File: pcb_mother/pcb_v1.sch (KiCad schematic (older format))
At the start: 32 parts, among them J1 Conn_01x02, J10 Conn_01x02, J11 Conn_01x06, J12 Conn_01x02, J13 Conn_01x02, J14 Conn_01x06, J3 Conn_01x02, J4 Conn_01x02_Male, J5 Conn_01x02_Male, J6 Conn_01x02, J7 Conn_01x01, J8 Conn_01x01, J9 Conn_01x02, Q10 2N2219, Q11 2N2219, Q12 2N2219, Q13 2N2219, Q14 2N2219, U1 TB6612F, U2 Rws433mhz, U3 tws

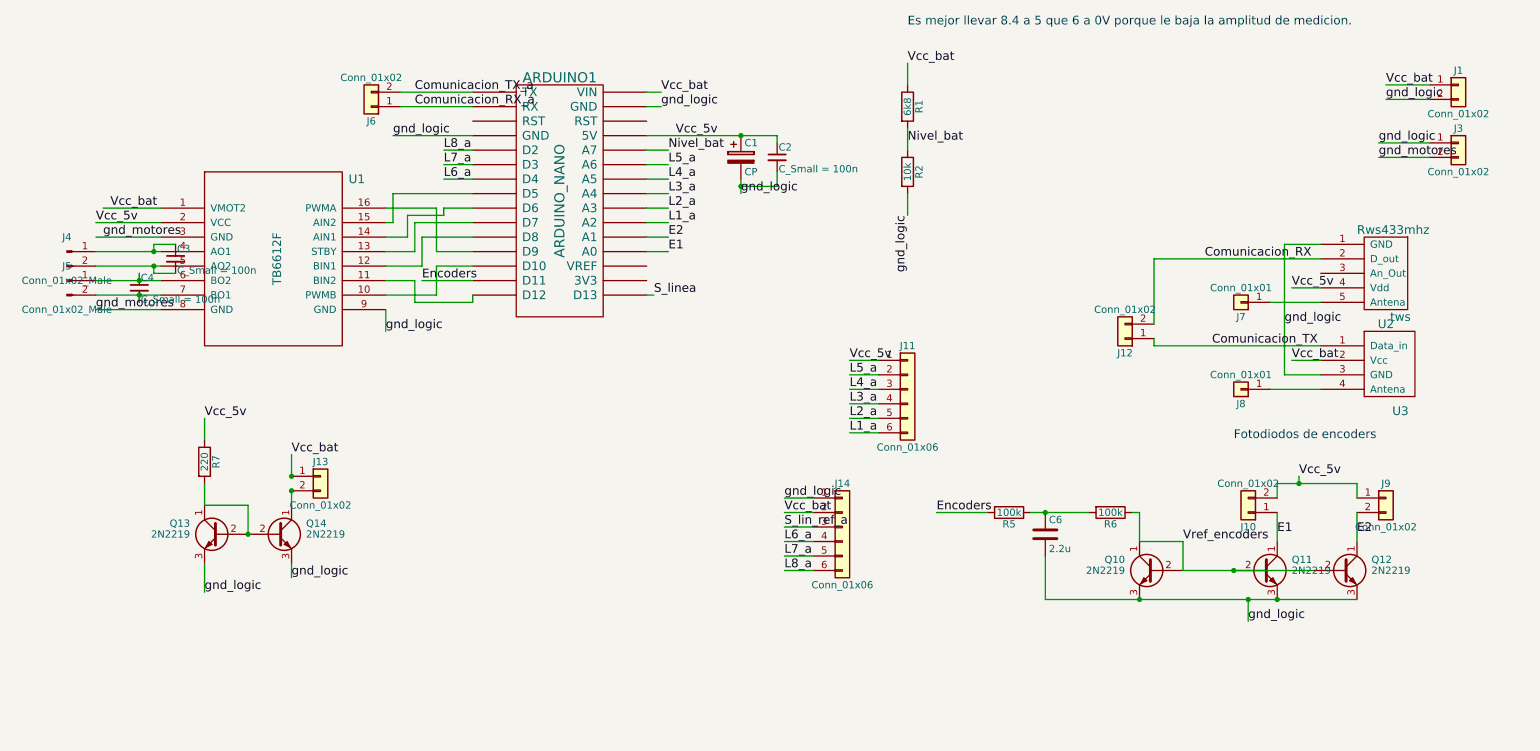
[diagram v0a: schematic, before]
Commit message: Se moifico el esquematico y se esta acomodando para poder armar el pcb, la linea que se va a seguir es priorizar el funcionamiento antes que la estetica y el espacio.
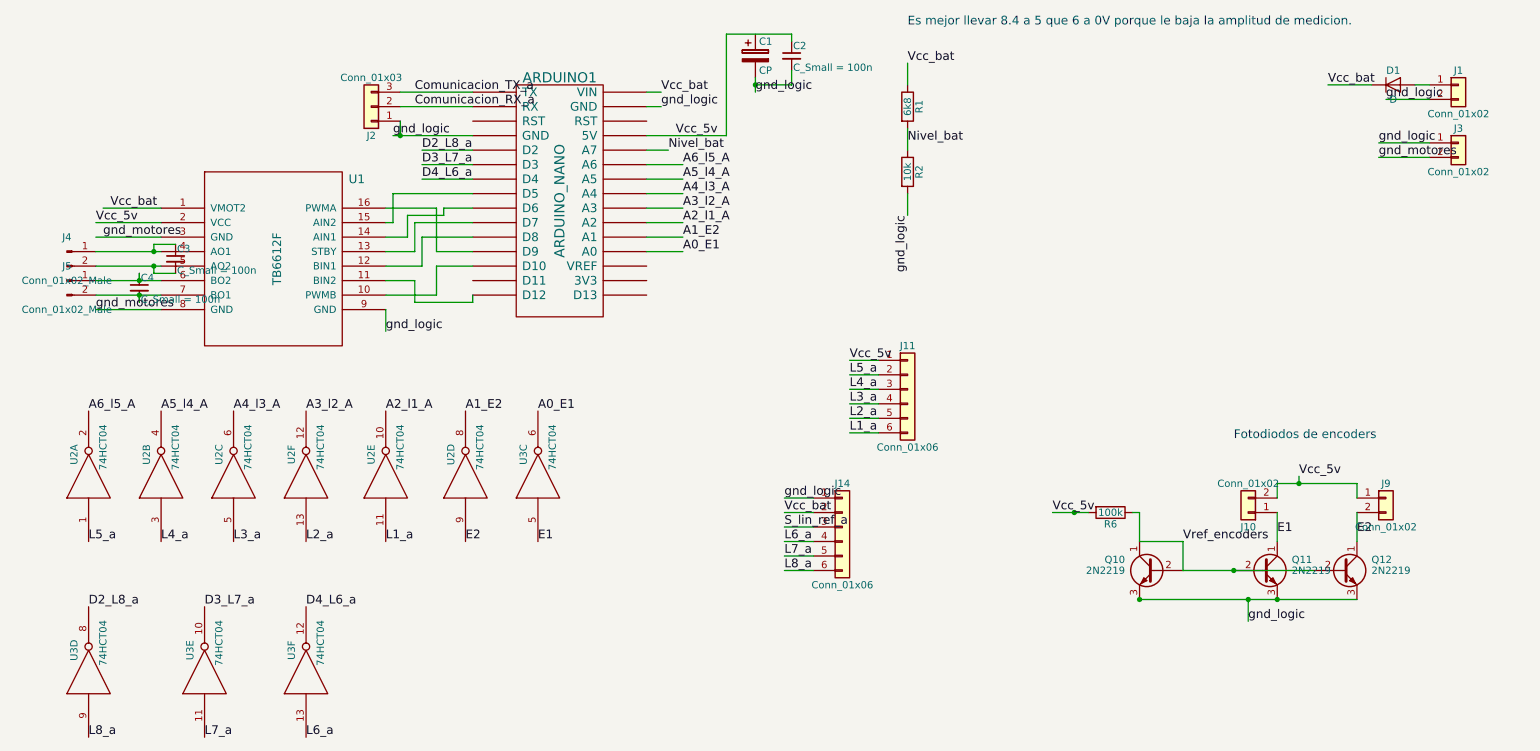
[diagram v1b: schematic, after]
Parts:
- removed C6: 2.2u, Capacitors_THT:CP_Radial_D5.0mm_P2.50mm, symbol C
- removed J12, J13, J6: Conn_01x02, Pin_Headers:Pin_Header_Straight_1x02_Pitch2.54mm, symbol Conn_01x02
- removed J7, J8: Conn_01x01, Pin_Headers:Pin_Header_Straight_1x01_Pitch2.54mm, symbol Conn_01x01
- removed Q13, Q14: 2N2219, TO_SOT_Packages_THT:TO-92_Inline_Wide, symbol BC548
- removed R5: 100k, Resistors_THT:R_Axial_DIN0207_L6.3mm_D2.5mm_P10.16mm_Horizontal, symbol R
- removed R7: 220, Resistors_THT:R_Axial_DIN0207_L6.3mm_D2.5mm_P10.16mm_Horizontal, symbol R
- removed U2: Rws433mhz, Propias:rws433, symbol Rws433mhz
- removed U3: tws, Propias:tws433, symbol tws
- added D1: D, Diodes_SMD:D_1206, symbol D
- added J2: Conn_01x03, Pin_Headers:Pin_Header_Straight_1x03_Pitch2.54mm, symbol Conn_01x03
- added U2, U3: 74HCT04, Housings_DIP:DIP-14_W7.62mm_Socket_LongPads, symbol 74HCT04
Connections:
- net Comunicacion_RX_a: now also J2.2 (Pin_2)
- net Comunicacion_TX_a: now also J2.3 (Pin_3)
- net E1: now also U3.5; no longer ARDUINO1.19 (A0)
- net E2: now also U2.9; no longer ARDUINO1.20 (A1)
- net L1_a: now also U2.11; no longer ARDUINO1.21 (A2)
- net L2_a: now also U2.13; no longer ARDUINO1.22 (A3)
- net L3_a: now also U2.5; no longer ARDUINO1.23 (A4)
- net L4_a: now also U2.3; no longer ARDUINO1.24 (A5)
- net L5_a: now also U2.1; no longer ARDUINO1.25 (A6)
- net L6_a: now also U3.13; no longer ARDUINO1.7 (D4)
- net L7_a: now also U3.11; no longer ARDUINO1.6 (D3)
- net L8_a: now also U3.9; no longer ARDUINO1.5 (D2)
- net Vcc_5v: now also R6.2; no longer C1.1
- net Vcc_bat: now also D1.1 (K); no longer J1.1 (Pin_1)
- net gnd_logic: now also J2.1 (Pin_1)
- net Encoders: no longer names the net of ARDUINO1.14 (D11)
- net S_linea: no longer names the net of ARDUINO1.16 (D13)
- new net: D1.2 (A), J1.1 (Pin_1)
- new net A0_E1: ARDUINO1.19 (A0), U3.6
- new net A1_E2: ARDUINO1.20 (A1), U2.8
- new net A2_l1_A: ARDUINO1.21 (A2), U2.10
- new net A3_l2_A: ARDUINO1.22 (A3), U2.12
- new net A4_l3_A: ARDUINO1.23 (A4), U2.6
- new net A5_l4_A: ARDUINO1.24 (A5), U2.4
- new net A6_l5_A: ARDUINO1.25 (A6), U2.2
- new net D2_L8_a: ARDUINO1.5 (D2), U3.8
- new net D3_L7_a: ARDUINO1.6 (D3), U3.10
- new net D4_L6_a: ARDUINO1.7 (D4), U3.12
- new net GND: U2.7 (GND), U2.7 (GND), U2.7 (GND), U2.7 (GND), U2.7 (GND), U2.7 (GND), U3.7 (GND), U3.7 (GND), U3.7 (GND), U3.7 (GND)
- new net VCC: U2.14 (VCC), U2.14 (VCC), U2.14 (VCC), U2.14 (VCC), U2.14 (VCC), U2.14 (VCC), U3.14 (VCC), U3.14 (VCC), U3.14 (VCC), U3.14 (VCC)
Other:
- moved on the sheet: C1, C2

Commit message: Se pudiron acomodar los inversores, ahora falta poner el divisor resistivo, los planos de tierra, los puentes y los aujeros...
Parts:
- renumbered U2 to U3
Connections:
- net Vcc_5v is gone; now on net VCC: ARDUINO1.27 (5V), C2.1, J10.2 (Pin_2), J11.1 (Pin_1), J9.1 (Pin_1), R6.2, U1.2 (VCC)
- net A0_E1: now also U3.4; no longer U3.6
- net A1_E2: now also U3.6; no longer U3.8
- net E1: now also J9.2 (Pin_2), Q12.1 (C); no longer J10.1 (Pin_1), Q11.1 (C)
- net E2: now also J10.1 (Pin_1), Q11.1 (C), U3.3; no longer J9.2 (Pin_2), Q12.1 (C), U3.9
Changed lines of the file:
@@
 	9600 4050 9600 4250
 Connection ~ 9050 4650
-Text Label 9600 4200 0    60   ~ 0
+Text Label 9050 4150 0    60   ~ 0
 E2
-Text Label 9050 4200 0    60   ~ 0
+Text Label 9600 4150 0    60   ~ 0
 E1
 $Comp
@@
 Text Label 2900 3350 0    60   ~ 0
 A2_l1_A
+Text Label 3950 3350 0    60   ~ 0
+A1_E2
 Text Label 3450 3350 0    60   ~ 0
-A1_E2
-Text Label 3950 3350 0    60   ~ 0
 A0_E1
 Text Label 850  4700 0    60   ~ 0
@@
 $EndComp
 $Comp
-L 74HCT04 U2
-U 4 1 5AF29DC5
+L 74HCT04 U3
+U 2 1 5AF29DC5
 P 3450 3800
-F 0 "U2" H 3600 3900 50  0000 C CNN
+F 0 "U3" H 3600 3900 50  0000 C CNN
 F 1 "74HCT04" H 3650 3700 50  0000 C CNN
 F 2 "Housings_DIP:DIP-14_W7.62mm_Socket_LongPads" H 3450 3800 50  0001 C CNN
 F 3 "" H 3450 3800 50  0001 C CNN
-	4    3450 3800
+	2    3450 3800
 	0    -1   -1   0
 $EndComp
@@
 Text Label 4950 1650 0    60   ~ 0
 A6_l5_A
+Text Label 5250 1450 0    60   ~ 0
+VCC
 $EndSCHEMATC

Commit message: Casi termino la placa, falta el plano de tierra, algunos puentes y los aujeros de montaje.
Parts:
- C1: value CP -> 10u
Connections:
- net gnd_logic is gone; now on net GND: ARDUINO1.29 (GND), ARDUINO1.4 (GND), C1.2, C2.2, J1.2 (Pin_2), J14.1 (Pin_1), J2.1 (Pin_1), J3.1 (Pin_1), Q10.3 (E), Q11.3 (E), Q12.3 (E), R2.2, U1.9 (GND)
- net VCC: now also C1.1
- net S_lin_ref_a: no longer names the net of J14.3 (Pin_3)
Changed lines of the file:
@@
 P 5450 900
 F 0 "C1" H 5475 1000 50  0000 L CNN
-F 1 "CP" H 5475 800 50  0000 L CNN
+F 1 "10u" H 5475 800 50  0000 L CNN
 F 2 "Capacitors_THT:CP_Radial_D5.0mm_P2.50mm" H 5488 750 50  0001 C CNN
 F 3 "" H 5450 900 50  0001 C CNN
@@
 Wire Wire Line
 	6100 3200 6300 3200
-Text Label 5650 4150 0    60   ~ 0
-S_lin_ref_a
 Wire Wire Line
 	5650 4450 5850 4450
@@
 Text Label 5250 1450 0    60   ~ 0
 VCC
+Wire Wire Line
+	5400 750  5450 750
+Connection ~ 5450 750
+Connection ~ 5400 750
+Text Label 5700 1100 0    60   ~ 0
+GND
 $EndSCHEMATC

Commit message: se realiza un ultimo chekeo antes de la imprecion.
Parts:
- D1: footprint Diodes_SMD:D_1206 -> Diodes_THT:D_DO-35_SOD27_P7.62mm_Horizontal
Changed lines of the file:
@@
 F 0 "D1" H 9850 1200 50  0000 C CNN
 F 1 "D" H 9850 1000 50  0000 C CNN
-F 2 "Diodes_SMD:D_1206" H 9850 1100 50  0001 C CNN
+F 2 "Diodes_THT:D_DO-35_SOD27_P7.62mm_Horizontal" H 9850 1100 50  0001 C CNN
 F 3 "" H 9850 1100 50  0001 C CNN
 	1    9850 1100
@@
 Wire Wire Line
 	9600 4650 8100 4650
-Text Label 7500 4050 0    60   ~ 0
+Text Label 7300 4050 0    60   ~ 0
 Vcc_5v
-Wire Wire Line
-	7500 4050 7750 4050
-Connection ~ 7650 4050
 Wire Wire Line
 	4700 1450 5250 1450
@@
 Text Label 5700 1100 0    60   ~ 0
 GND
+Wire Wire Line
+	7750 4050 7300 4050
 $EndSCHEMATC
